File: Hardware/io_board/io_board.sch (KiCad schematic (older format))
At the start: 28 parts, among them J1 Conn_01x40, J2 Conn_02x05_Odd_Even, J3 Mini-DIN-6, J4 Conn_02x10_Odd_Even, U1 74LS137, U2 W65C22NxP

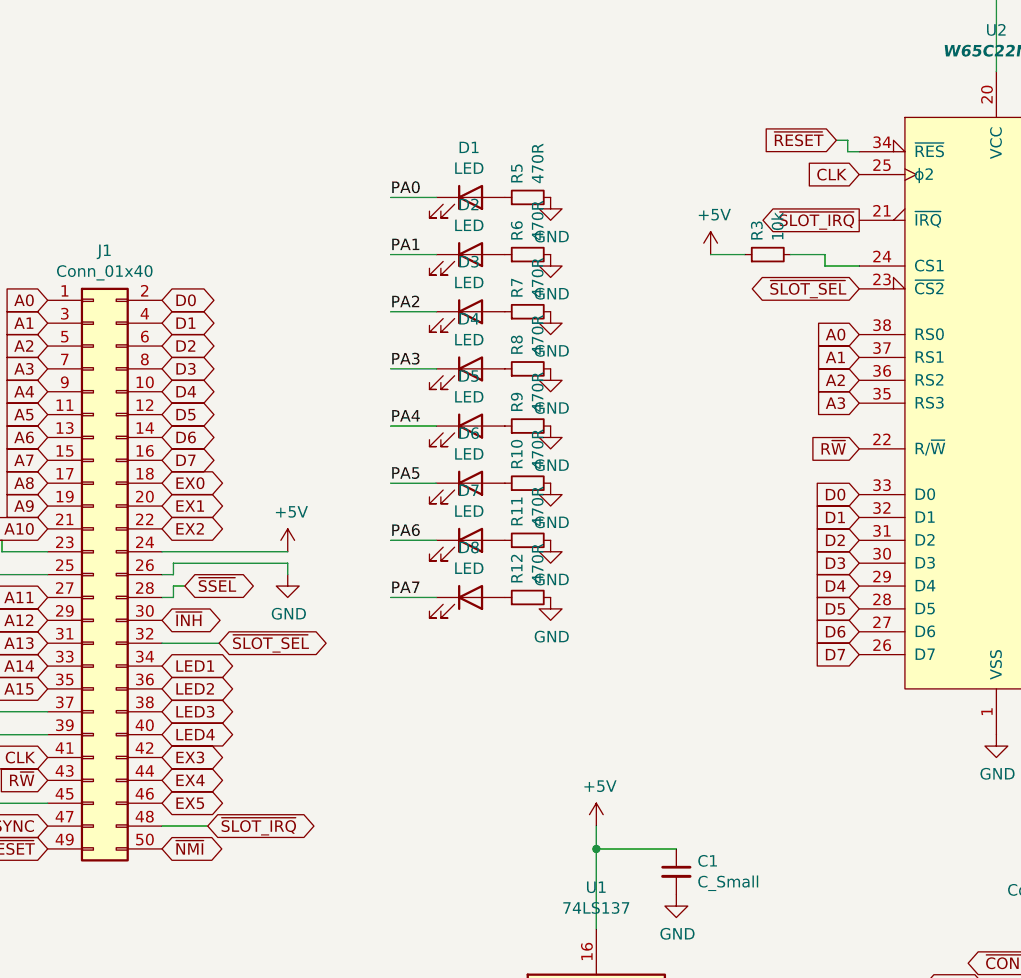
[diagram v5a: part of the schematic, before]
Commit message: Many updates. SLOW signal is now shared amongst all slots, so their output has to be open drain.
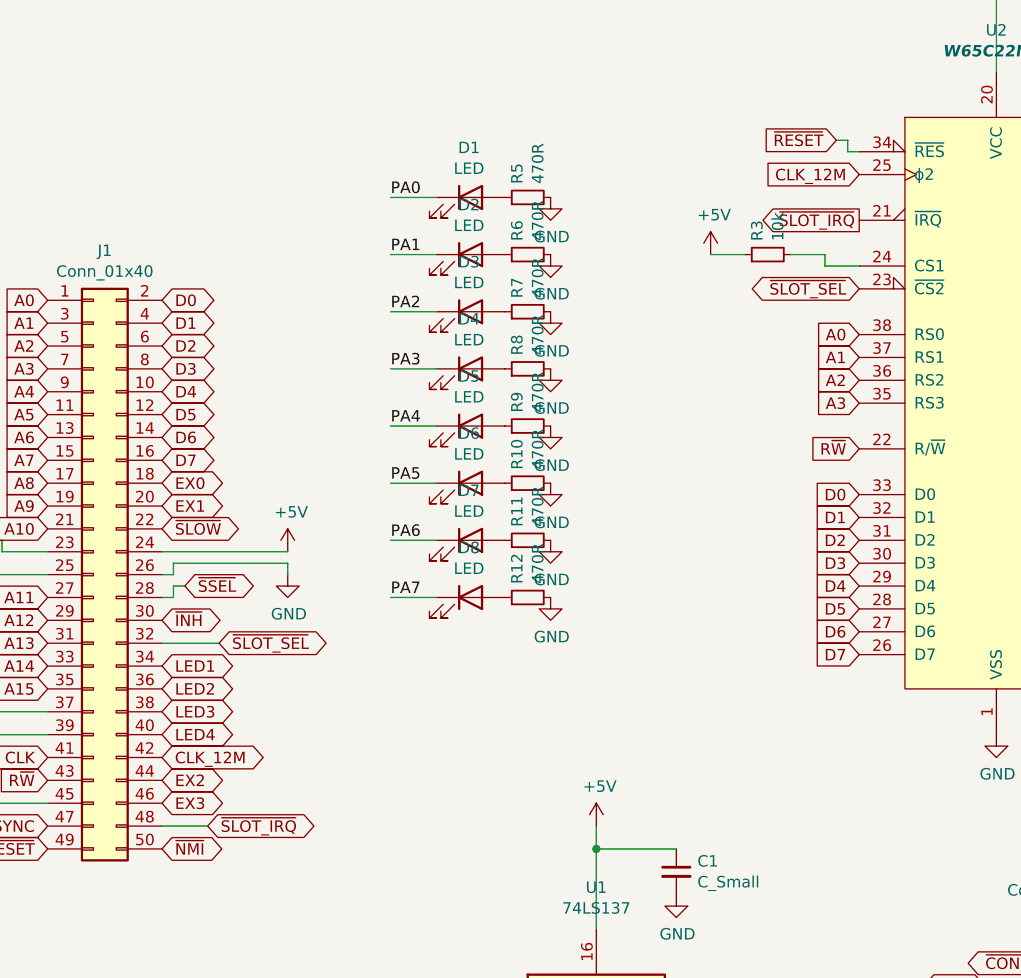
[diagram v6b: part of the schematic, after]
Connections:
- net EX4 is gone; now on net EX2: J1.44 (Pin_44)
- net EX5 is gone; now on net EX3: J1.46 (Pin_46)
- net CLK: no longer U2.25 (ϕ2)
- net EX2: no longer J1.22 (Pin_22)
- net EX3: no longer J1.42 (Pin_42)
- new net CLK_12M: J1.42 (Pin_42), U2.25 (ϕ2)
- new net ~SLOW~: J1.22 (Pin_22)
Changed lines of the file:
@@
 ~SLOT_IRQ~
 Text GLabel 2800 4450 2    50   BiDi ~ 0
-EX5
+EX3
 Text GLabel 2800 4350 2    50   BiDi ~ 0
-EX4
+EX2
 Text GLabel 2800 4250 2    50   BiDi ~ 0
-EX3
+CLK_12M
 Wire Wire Line
 	1750 4450 2300 4450
@@
 EX1
 Text GLabel 2800 3250 2    50   BiDi ~ 0
-EX2
+~SLOW~
 $Comp
 L 65xx:W65C22NxP U2
@@
 R~W~
 Text GLabel 5850 1700 0    50   Input ~ 0
-CLK
+CLK_12M
 Text GLabel 5750 1550 0    50   Input ~ 0
 ~RESET~

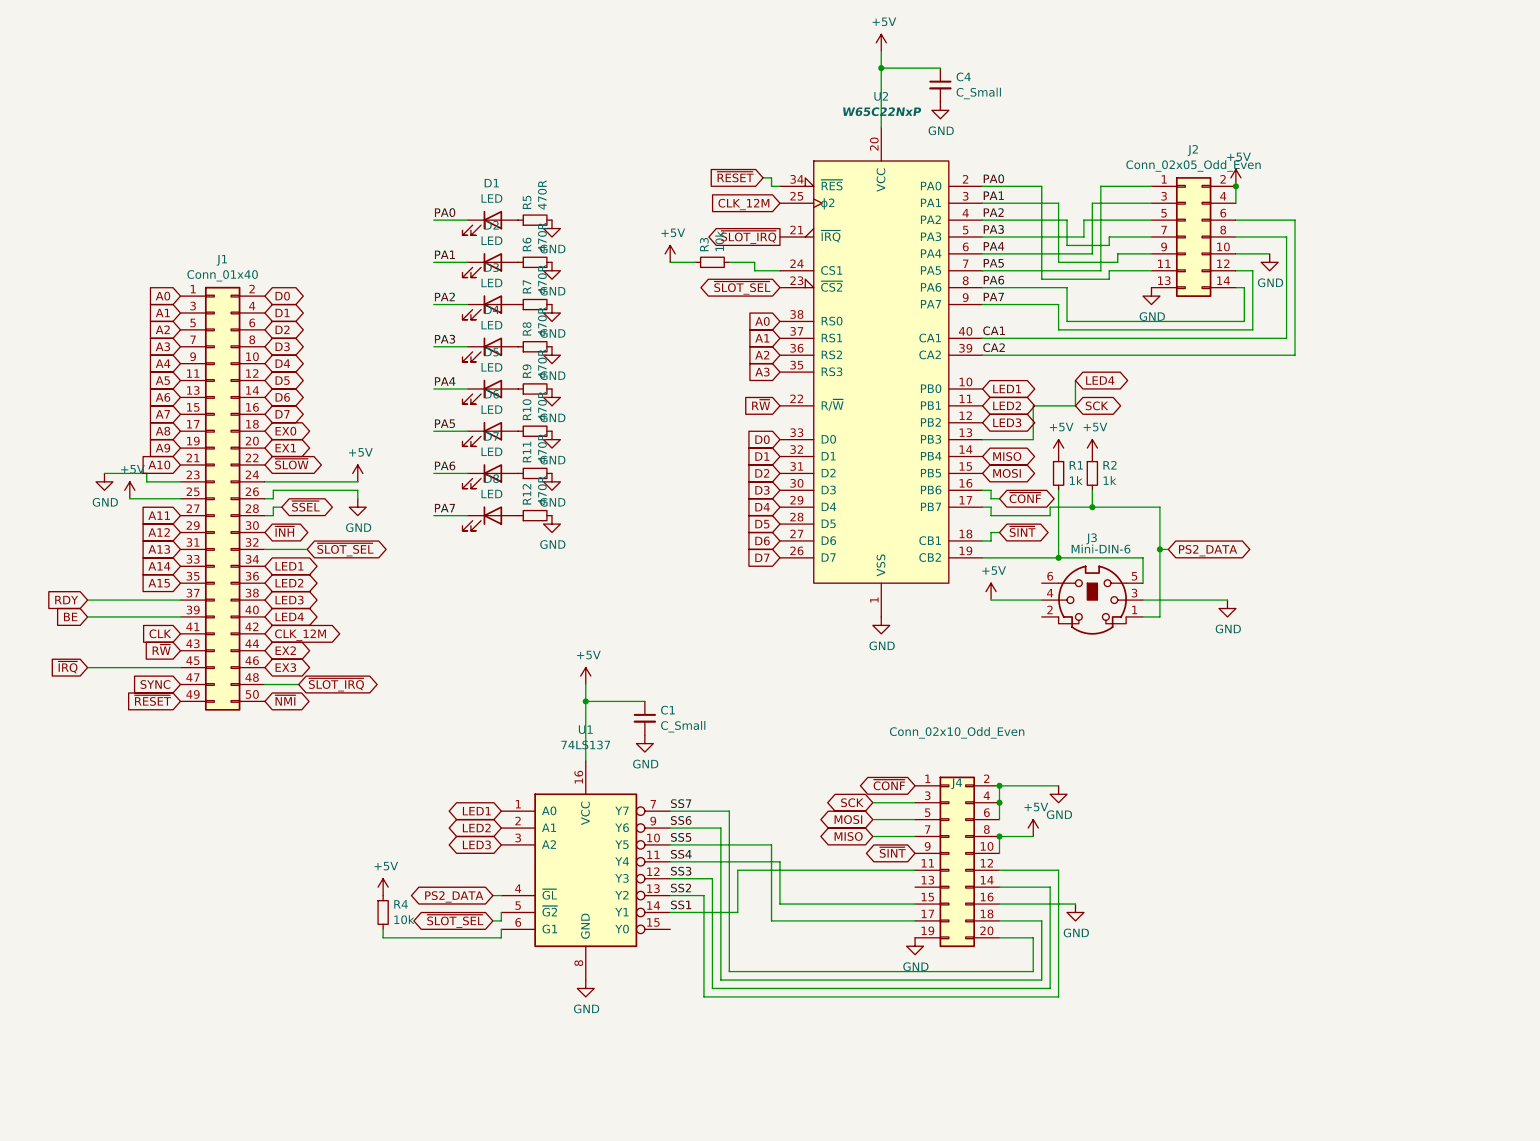
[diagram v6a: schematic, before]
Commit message: [WIP] add 74HS14 schmitt trigger inverter to PS/2 data and clock signals
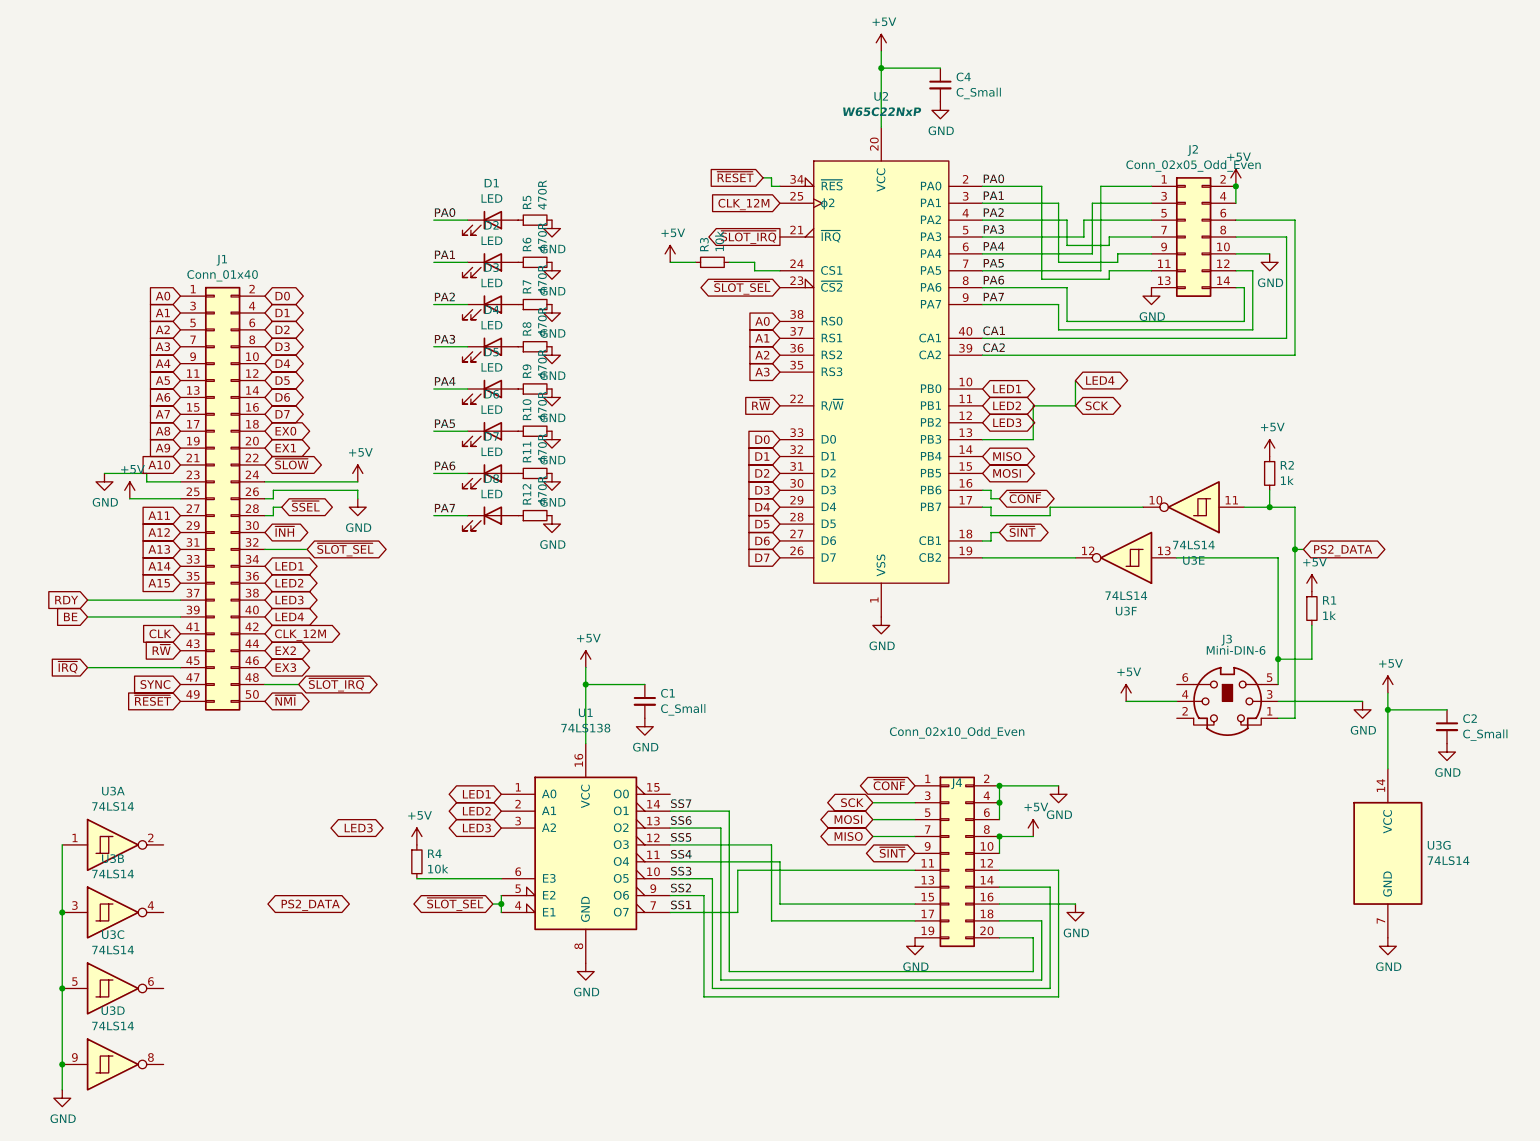
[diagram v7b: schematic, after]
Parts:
- removed U1: 74LS137, Package_DIP:DIP-16_W7.62mm_Socket, symbol 74xx:74LS137
- added C2: C_Small, Capacitor_SMD:C_1206_3216Metric_Pad1.42x1.75mm_HandSolder, symbol Device:C_Small
- added U1: 74LS138, Package_DIP:DIP-16_W7.62mm_Socket, symbol 74xx:74LS138
- added U3: 74LS14, Package_DIP:DIP-14_W7.62mm_Socket, symbol 74xx:74LS14
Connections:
- net +5V: now also C2.1, U1.16 (VCC), U3.14 (VCC)
- net GND: now also C2.2, U1.8 (GND), U3.1, U3.3, U3.5, U3.7 (GND), U3.9
- net LED1: now also U1.1 (A0)
- net LED2: now also U1.2 (A1)
- net LED3: now also U1.3 (A2)
- net PS2_DATA: now also U3.11; no longer U2.17 (PB7)
- net SS1: now also U1.7 (O7)
- net SS2: now also U1.9 (O6)
- net SS3: now also U1.10 (O5)
- net SS4: now also U1.11 (O4)
- net SS5: now also U1.12 (O3)
- net SS6: now also U1.13 (O2)
- net SS7: now also U1.14 (O1)
- net ~SLOT_SEL~: now also U1.4 (E1), U1.5 (E2)
- net at J3.5, R1.2: now also U3.13; no longer U2.19 (CB2)
- net at R4.2: now also U1.6 (E3)
- new net: U2.17 (PB7), U3.10
- new net: U2.19 (CB2), U3.12
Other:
- moved on the sheet: C1, J3, R1, R2, R4

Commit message: small fixes on the hardware
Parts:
- added C3: C_Small, Capacitor_SMD:C_1206_3216Metric_Pad1.42x1.75mm_HandSolder, symbol Device:C_Small
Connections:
- net +5V: now also C3.1
- net GND: now also C3.2; no longer C2.2, U3.1, U3.3
- net PS2_DATA: now also U3.13; no longer U3.11
- net at U2.19 (CB2): now also U3.4; no longer U3.12
- net at J3.5, R1.2: now also U3.1; no longer U3.13
- net at U3.2: now also U3.3
- new net: U3.11, U3.12
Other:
- moved on the sheet: U3A, U3B, U3E, U3F
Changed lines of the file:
@@
 $EndComp
 Wire Wire Line
-	8200 4650 7900 4650
+	8200 4650 8000 4650
 Wire Wire Line
 	8800 4750 8900 4750
@@
 	7100 3400 7050 3400
 Wire Wire Line
-	7450 3500 7450 3550
-Wire Wire Line
 	7450 3550 7100 3550
 Wire Wire Line
@@
 L 74xx:74LS14 U3
 U 1 1 601A49CD
-P 1900 5500
-F 0 "U3" H 1900 5817 50  0000 C CNN
-F 1 "74LS14" H 1900 5726 50  0000 C CNN
-F 2 "Package_DIP:DIP-14_W7.62mm_Socket" H 1900 5500 50  0001 C CNN
-F 3 "http://www.ti.com/lit/gpn/sn74LS14" H 1900 5500 50  0001 C CNN
-	1    1900 5500
-	1    0    0    -1
+P 8250 3900
+F 0 "U3" H 8250 4217 50  0000 C CNN
+F 1 "74LS14" H 8250 4126 50  0000 C CNN
+F 2 "Package_DIP:DIP-14_W7.62mm_Socket" H 8250 3900 50  0001 C CNN
+F 3 "http://www.ti.com/lit/gpn/sn74LS14" H 8250 3900 50  0001 C CNN
+	1    8250 3900
+	-1   0    0    1
 $EndComp
 $Comp
 L 74xx:74LS14 U3
 U 2 1 601A559B
-P 1900 5900
-F 0 "U3" H 1900 6217 50  0000 C CNN
-F 1 "74LS14" H 1900 6126 50  0000 C CNN
-F 2 "Package_DIP:DIP-14_W7.62mm_Socket" H 1900 5900 50  0001 C CNN
-F 3 "http://www.ti.com/lit/gpn/sn74LS14" H 1900 5900 50  0001 C CNN
-	2    1900 5900
-	1    0    0    -1
+P 7450 3900
+F 0 "U3" H 7450 4217 50  0000 C CNN
+F 1 "74LS14" H 7450 4126 50  0000 C CNN
+F 2 "Package_DIP:DIP-14_W7.62mm_Socket" H 7450 3900 50  0001 C CNN
+F 3 "http://www.ti.com/lit/gpn/sn74LS14" H 7450 3900 50  0001 C CNN
+	2    7450 3900
+	-1   0    0    1
 $EndComp
 $Comp
@@
 L 74xx:74LS14 U3
 U 5 1 601A824E
+P 7750 3400
+F 0 "U3" H 7750 3717 50  0000 C CNN
+F 1 "74LS14" H 7750 3626 50  0000 C CNN
+F 2 "Package_DIP:DIP-14_W7.62mm_Socket" H 7750 3400 50  0001 C CNN
+F 3 "http://www.ti.com/lit/gpn/sn74LS14" H 7750 3400 50  0001 C CNN
+	5    7750 3400
+	-1   0    0    1
+$EndComp
+$Comp
+L 74xx:74LS14 U3
+U 6 1 601A8ACA
 P 8300 3500
 F 0 "U3" H 8300 3817 50  0000 C CNN
@@
 F 2 "Package_DIP:DIP-14_W7.62mm_Socket" H 8300 3500 50  0001 C CNN
 F 3 "http://www.ti.com/lit/gpn/sn74LS14" H 8300 3500 50  0001 C CNN
-	5    8300 3500
-	-1   0    0    1
-$EndComp
-$Comp
-L 74xx:74LS14 U3
-U 6 1 601A8ACA
-P 7900 3800
-F 0 "U3" H 7900 4117 50  0000 C CNN
-F 1 "74LS14" H 7900 4026 50  0000 C CNN
-F 2 "Package_DIP:DIP-14_W7.62mm_Socket" H 7900 3800 50  0001 C CNN
-F 3 "http://www.ti.com/lit/gpn/sn74LS14" H 7900 3800 50  0001 C CNN
-	6    7900 3800
+	6    8300 3500
 	-1   0    0    1
 $EndComp
@@
 	8900 3500 8750 3500
 Wire Wire Line
-	7450 3500 8000 3500
-Wire Wire Line
 	8750 3400 8750 3500
 Connection ~ 8750 3500
@@
 Connection ~ 8800 4400
 Wire Wire Line
-	8800 4400 8800 3800
-Wire Wire Line
-	8800 3800 8200 3800
-Wire Wire Line
-	7050 3800 7600 3800
+	8800 4400 8800 3900
 $Comp
 L power:+5V #PWR0132
@@
 L power:GND #PWR0133
 U 1 1 6023E74F
-P 9800 4900
-F 0 "#PWR0133" H 9800 4650 50  0001 C CNN
-F 1 "GND" H 9805 4727 50  0000 C CNN
-F 2 "" H 9800 4900 50  0001 C CNN
-F 3 "" H 9800 4900 50  0001 C CNN
-	1    9800 4900
+P 8000 4950
+F 0 "#PWR0133" H 8000 4700 50  0001 C CNN
+F 1 "GND" H 8005 4777 50  0000 C CNN
+F 2 "" H 8000 4950 50  0001 C CNN
+F 3 "" H 8000 4950 50  0001 C CNN
+	1    8000 4950
 	1    0    0    -1
 $EndComp
@@
 $EndComp
 Wire Wire Line
-	1600 5500 1600 5900
-Connection ~ 1600 5900
-Wire Wire Line
-	1600 5900 1600 6350
-Connection ~ 1600 6350
-Wire Wire Line
 	1600 6350 1600 6800
 Connection ~ 1600 6800
@@
 	4200 5900 4200 5850
 Connection ~ 4200 5850
+$Comp
+L Device:C_Small C3
+U 1 1 604850AB
+P 8000 4850
+F 0 "C3" H 8092 4896 50  0000 L CNN
+F 1 "C_Small" H 8092 4805 50  0000 L CNN
+F 2 "Capacitor_SMD:C_1206_3216Metric_Pad1.42x1.75mm_HandSolder" H 8000 4850 50  0001 C CNN
+F 3 "~" H 8000 4850 50  0001 C CNN
+	1    8000 4850
+	1    0    0    -1
+$EndComp
+Wire Wire Line
+	8000 4750 8000 4650
+Connection ~ 8000 4650
+Wire Wire Line
+	8000 4650 7900 4650
+Wire Wire Line
+	8050 3400 8050 3450
+Wire Wire Line
+	8050 3450 8000 3450
+Wire Wire Line
+	8000 3450 8000 3500
+Wire Wire Line
+	7450 3400 7450 3550
+Wire Wire Line
+	8550 3900 8800 3900
+Connection ~ 8800 3900
+Wire Wire Line
+	8800 3900 8800 3800
+Wire Wire Line
+	7950 3900 7750 3900
+Wire Wire Line
+	7150 3900 7100 3900
+Wire Wire Line
+	7100 3900 7100 3800
+Wire Wire Line
+	7100 3800 7050 3800
 $EndSCHEMATC
